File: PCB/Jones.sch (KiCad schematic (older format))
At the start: 246 parts, among them J1 USB_C_Receptacle_USB2.0, J2 Conn_01x03, J3 Conn_01x02, J5 Conn_02x03_Odd_Even, U1 ATmega32U4-AU, U2 24LC64, Y1 16MHz

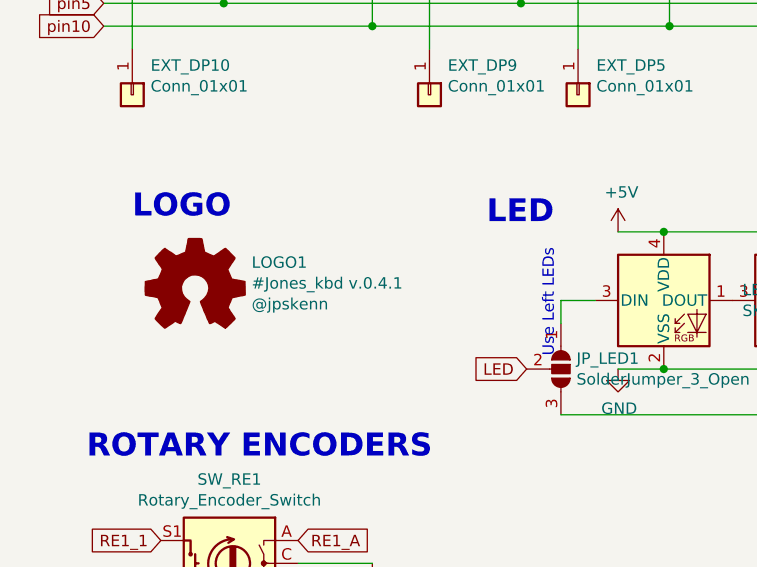
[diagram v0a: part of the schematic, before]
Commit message: 世界市民メッセージ追加。バージョン表記更新
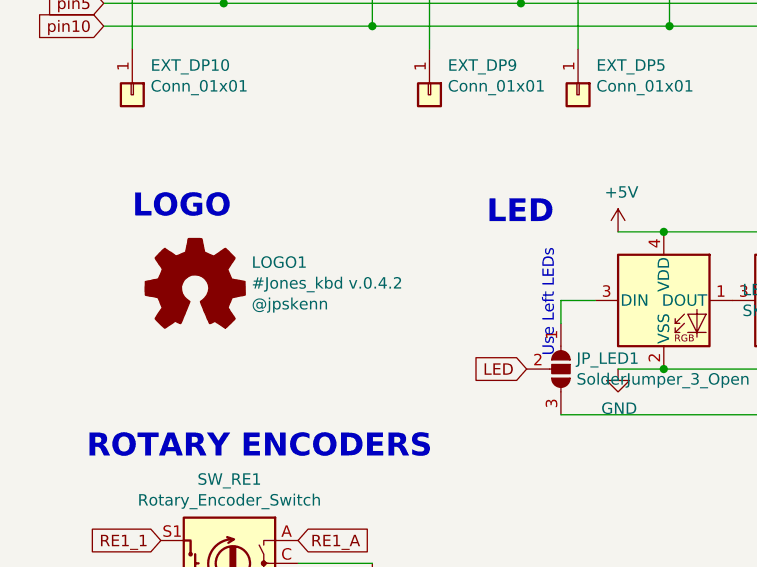
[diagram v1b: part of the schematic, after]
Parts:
- LOGO1: value #Jones_kbd v.0.4.1 -> #Jones_kbd v.0.4.2
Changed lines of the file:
@@
 Sheet 1 1
 Title "Jones"
-Date "2021-06-27"
-Rev "v.0.4.1"
+Date "2021-08-01"
+Rev "v.0.4.2"
 Comp "@jpskenn"
 Comment1 ""
@@
 P 1200 8675
 F 0 "LOGO1" H 1447 8791 50  0000 L CNN
-F 1 "#Jones_kbd v.0.4.1" H 1447 8700 50  0000 L CNN
+F 1 "#Jones_kbd v.0.4.2" H 1447 8700 50  0000 L CNN
 F 2 "locallib:Jones_logo_7.8x13.2" H 1200 8675 50  0001 C CNN
 F 3 "~" H 1200 8675 50  0001 C CNN

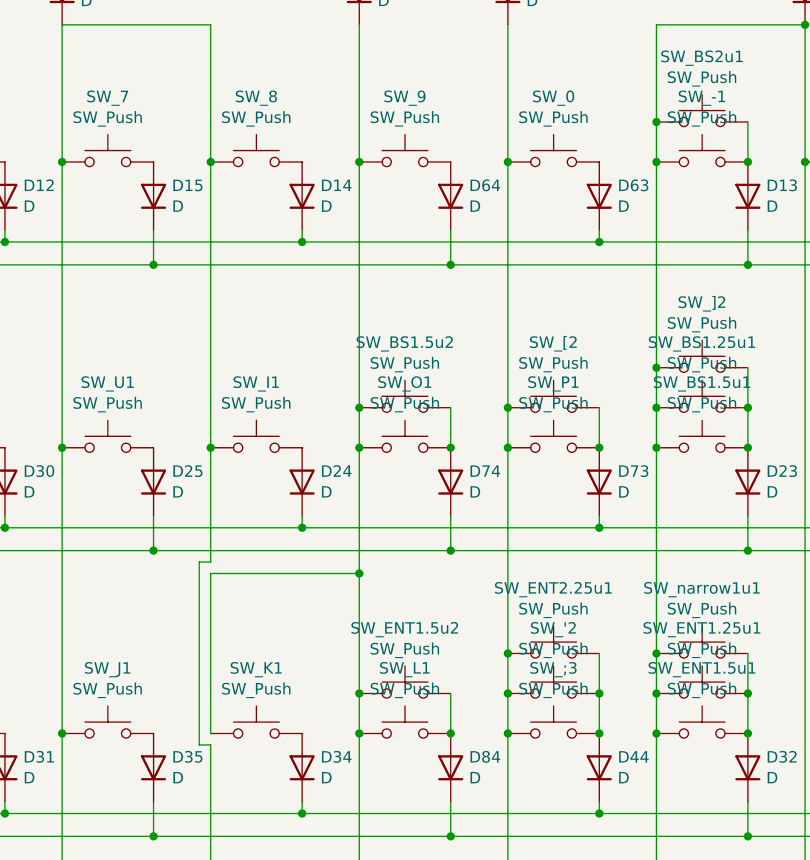
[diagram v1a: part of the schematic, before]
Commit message: Narrowレイアウトを、104USと108JPキーキャップに対応
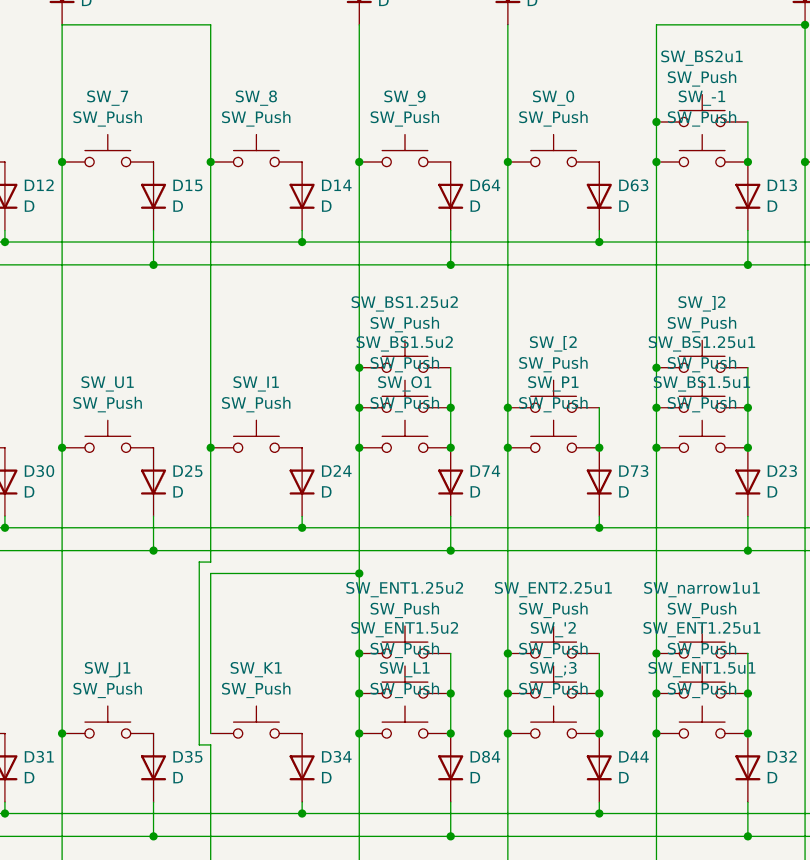
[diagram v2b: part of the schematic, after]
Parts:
- added SW_BS1.25u2, SW_ENT1.25u2: SW_Push, MX_Alps_Hybrid:MXOnly-1.25U-Hotswap-guide-Rotate, symbol Switch:SW_Push
- SW_BS1.5u2, SW_ENT1.5u2: footprint MX_Alps_Hybrid:MXOnly-1.5U-Hotswap-guide -> MX_Alps_Hybrid:MXOnly-1.5U-Hotswap-guide-Rotate
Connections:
- wire segments 427 -> 431
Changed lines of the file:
@@
 F 0 "SW_BS1.5u2" H 8275 3435 50  0000 C CNN
 F 1 "SW_Push" H 8275 3344 50  0000 C CNN
-F 2 "MX_Alps_Hybrid:MXOnly-1.5U-Hotswap-guide" H 8275 3350 50  0001 C CNN
+F 2 "MX_Alps_Hybrid:MXOnly-1.5U-Hotswap-guide-Rotate" H 8275 3350 50  0001 C CNN
 F 3 "~" H 8275 3350 50  0001 C CNN
 	1    8275 3150
@@
 	8075 3150 8075 3325
 Wire Wire Line
-	8075 2075 8075 3150
+	8075 2075 8075 2975
 $Comp
 L Switch:SW_Push SW_ENT1.5u2
@@
 F 0 "SW_ENT1.5u2" H 8275 4685 50  0000 C CNN
 F 1 "SW_Push" H 8275 4594 50  0000 C CNN
-F 2 "MX_Alps_Hybrid:MXOnly-1.5U-Hotswap-guide" H 8275 4600 50  0001 C CNN
+F 2 "MX_Alps_Hybrid:MXOnly-1.5U-Hotswap-guide-Rotate" H 8275 4600 50  0001 C CNN
 F 3 "~" H 8275 4600 50  0001 C CNN
 	1    8275 4400
@@
 	9125 4225 9125 4400
 Wire Wire Line
-	8075 3875 8075 4400
+	8075 3875 8075 4225
 Connection ~ 8725 4225
 Wire Wire Line
@@
 	1    0    0    -1
 $EndComp
+$Comp
+L Switch:SW_Push SW_BS1.25u2
+U 1 1 61379E30
+P 8275 2975
+F 0 "SW_BS1.25u2" H 8275 3260 50  0000 C CNN
+F 1 "SW_Push" H 8275 3169 50  0000 C CNN
+F 2 "MX_Alps_Hybrid:MXOnly-1.25U-Hotswap-guide-Rotate" H 8275 3175 50  0001 C CNN
+F 3 "~" H 8275 3175 50  0001 C CNN
+	1    8275 2975
+	1    0    0    -1
+$EndComp
+Connection ~ 8075 2975
+Wire Wire Line
+	8075 2975 8075 3150
+Wire Wire Line
+	8475 2975 8475 3150
+Connection ~ 8475 3150
+$Comp
+L Switch:SW_Push SW_ENT1.25u2
+U 1 1 613DB418
+P 8275 4225
+F 0 "SW_ENT1.25u2" H 8275 4510 50  0000 C CNN
+F 1 "SW_Push" H 8275 4419 50  0000 C CNN
+F 2 "MX_Alps_Hybrid:MXOnly-1.25U-Hotswap-guide-Rotate" H 8275 4425 50  0001 C CNN
+F 3 "~" H 8275 4425 50  0001 C CNN
+	1    8275 4225
+	1    0    0    -1
+$EndComp
+Connection ~ 8075 4225
+Wire Wire Line
+	8075 4225 8075 4400
+Wire Wire Line
+	8475 4225 8475 4400
+Connection ~ 8475 4400
 $EndSCHEMATC

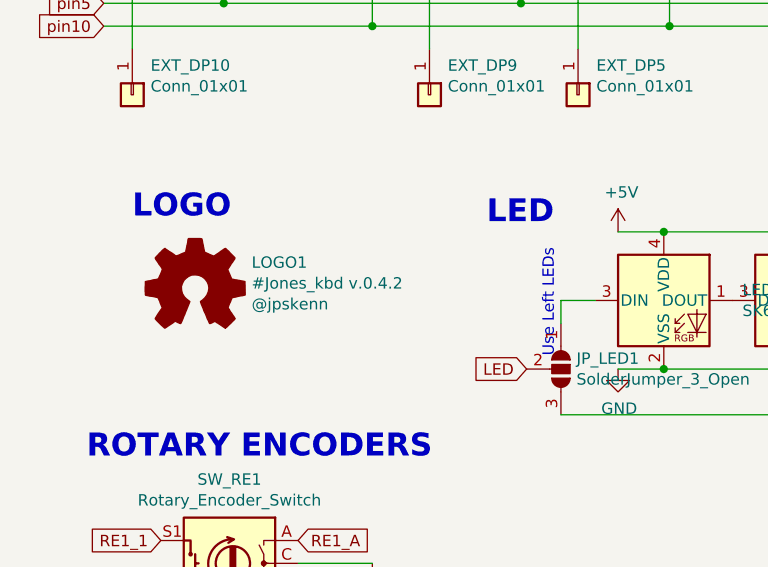
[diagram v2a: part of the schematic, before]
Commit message: バージョン表記変更
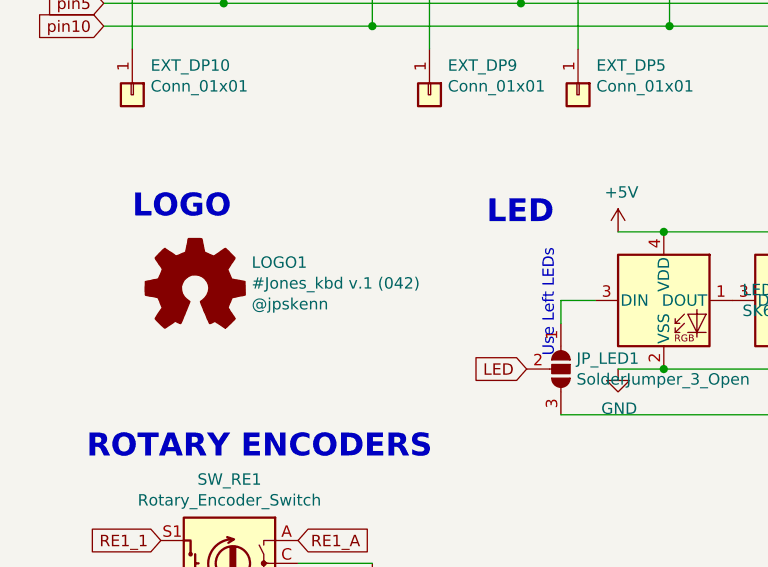
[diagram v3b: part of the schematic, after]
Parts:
- LOGO1: value #Jones_kbd v.0.4.2 -> #Jones_kbd v.1 (042)
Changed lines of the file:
@@
 Title "Jones"
 Date "2021-08-01"
-Rev "v.0.4.2"
+Rev "v.1 (042)"
 Comp "@jpskenn"
 Comment1 ""
@@
 P 1200 8675
 F 0 "LOGO1" H 1447 8791 50  0000 L CNN
-F 1 "#Jones_kbd v.0.4.2" H 1447 8700 50  0000 L CNN
+F 1 "#Jones_kbd v.1 (042)" H 1447 8700 50  0000 L CNN
 F 2 "locallib:Jones_logo_7.8x13.2" H 1200 8675 50  0001 C CNN
 F 3 "~" H 1200 8675 50  0001 C CNN

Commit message: 基板ロゴ更新
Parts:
- LOGO1: footprint locallib:Jones_logo_7.8x13.2 -> locallib:Jones_logo_B_R_60x98.2
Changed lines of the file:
@@
 F 0 "LOGO1" H 1447 8791 50  0000 L CNN
 F 1 "#Jones_kbd v.1 (042)" H 1447 8700 50  0000 L CNN
-F 2 "locallib:Jones_logo_7.8x13.2" H 1200 8675 50  0001 C CNN
+F 2 "locallib:Jones_logo_B_R_60x98.2" H 1200 8675 50  0001 C CNN
 F 3 "~" H 1200 8675 50  0001 C CNN
 F 4 "@jpskenn" H 1447 8609 50  0000 L CNN "Text"

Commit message: マトリクスのピン番号をQMKに合わせた
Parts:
- renumbered EXT_DP1 to EXT_DP0, EXT_DP2 to EXT_DP1, EXT_DP3 to EXT_DP2, EXT_DP4 to EXT_DP3, EXT_DP5 to EXT_DP4, EXT_DP6 to EXT_DP5, EXT_DP7 to EXT_DP6, EXT_DP8 to EXT_DP7, EXT_DP9 to EXT_DP8, EXT_DP10 to EXT_DP9, EXT_P1 to EXT_P0, EXT_P2 to EXT_P1, EXT_P3 to EXT_P2, EXT_P4 to EXT_P3, EXT_P5 to EXT_P4, EXT_P6 to EXT_P5, EXT_P7 to EXT_P6, EXT_P8 to EXT_P7, EXT_P9 to EXT_P8, EXT_P10 to EXT_P9
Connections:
- net labels added: pin0
- net labels removed: pin10
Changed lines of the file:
@@
 $EndComp
 Text GLabel 15275 2150 2    60   Input ~ 0
-pin6
-Text GLabel 15275 3750 2    60   Input ~ 0
 pin5
+Text GLabel 15275 3750 2    60   Input ~ 0
+pin4
 Text GLabel 15650 2450 2    50   Input ~ 0
-pin1
+pin0
 Wire Wire Line
 	13750 3450 14075 3450
@@
 $EndComp
 Text GLabel 800  2425 0    50   Input ~ 0
-pin1
+pin0
 Text GLabel 800  3675 0    50   Input ~ 0
-pin2
+pin1
 Text GLabel 800  4925 0    50   Input ~ 0
-pin3
+pin2
 Text GLabel 800  6175 0    50   Input ~ 0
-pin4
+pin3
 Text GLabel 800  7425 0    50   Input ~ 0
-pin5
+pin4
 Text GLabel 800  5025 0    50   Input ~ 0
-pin8
+pin7
 Text GLabel 800  6275 0    50   Input ~ 0
-pin9
+pin8
 Text GLabel 800  3775 0    50   Input ~ 0
-pin7
+pin6
 $Comp
 L Device:D D39
@@
 Connection ~ 9775 4575
 Text GLabel 4175 1175 1    50   Input ~ 0
-pin1
+pin0
 Text GLabel 10025 1175 1    50   Input ~ 0
-pin2
+pin1
 Text GLabel 6775 1175 1    50   Input ~ 0
-pin3
+pin2
 Text GLabel 8075 1175 1    50   Input ~ 0
-pin4
+pin3
 Text GLabel 2875 1175 1    50   Input ~ 0
-pin5
+pin4
 Text GLabel 6125 1175 1    50   Input ~ 0
-pin6
+pin5
 Text GLabel 8725 1175 1    50   Input ~ 0
-pin8
-Text GLabel 5475 1175 1    50   Input ~ 0
 pin7
-Text GLabel 800  2525 0    50   Input ~ 0
+Text GLabel 5475 1175 1    50   Input ~ 0
 pin6
+Text GLabel 800  2525 0    50   Input ~ 0
+pin5
 $Comp
 L Switch:SW_Push SW_RIGHT1
@@
 RE2_B
 Text GLabel 15275 2550 2    60   Input ~ 0
-pin9
-Text GLabel 15275 2850 2    60   Input ~ 0
 pin8
+Text GLabel 15275 2850 2    60   Input ~ 0
+pin7
 Connection ~ 3250 8425
 Wire Wire Line
@@
 AUDIO2
 Text GLabel 15275 4350 2    60   Input ~ 0
-pin3
+pin2
 Text GLabel 15275 4850 2    50   Input ~ 0
 RE2_A
@@
 LED
 Text GLabel 15275 3950 2    60   Input ~ 0
-pin4
+pin3
 Wire Wire Line
 	1325 2375 1325 2425
@@
 $EndComp
 Text GLabel 15275 4050 2    50   Input ~ 0
-pin10
+pin9
 Text GLabel 800  7525 0    50   Input ~ 0
-pin10
+pin9
 Wire Wire Line
 	800  2525 1975 2525
@@
 	800  7525 1975 7525
 Text GLabel 2225 1175 1    50   Input ~ 0
-pin9
+pin8
 $Comp
 L Device:D D9
@@
 $EndComp
 Text GLabel 925  1175 1    50   Input ~ 0
-pin10
+pin9
 $Comp
 L Device:D D42
@@
 SDA
 $Comp
-L Connector_Generic:Conn_01x01 EXT_P1
+L Connector_Generic:Conn_01x01 EXT_P0
 U 1 1 60A4B967
 P 10625 2425
-F 0 "EXT_P1" H 10705 2467 50  0000 L CNN
+F 0 "EXT_P0" H 10705 2467 50  0000 L CNN
 F 1 "Conn_01x01" H 10705 2376 50  0000 L CNN
 F 2 "TestPoint:TestPoint_THTPad_D1.5mm_Drill0.7mm" H 10625 2425 50  0001 C CNN
@@
 Connection ~ 10425 2425
 $Comp
-L Connector_Generic:Conn_01x01 EXT_P6
+L Connector_Generic:Conn_01x01 EXT_P5
 U 1 1 60A4CD39
 P 10625 2525
-F 0 "EXT_P6" H 10705 2567 50  0000 L CNN
+F 0 "EXT_P5" H 10705 2567 50  0000 L CNN
 F 1 "Conn_01x01" H 10705 2476 50  0000 L CNN
 F 2 "TestPoint:TestPoint_THTPad_D1.5mm_Drill0.7mm" H 10625 2525 50  0001 C CNN
@@
 Connection ~ 9775 2525
 $Comp
-L Connector_Generic:Conn_01x01 EXT_P2
+L Connector_Generic:Conn_01x01 EXT_P1
 U 1 1 60AB0114
 P 10625 3675
-F 0 "EXT_P2" H 10705 3717 50  0000 L CNN
+F 0 "EXT_P1" H 10705 3717 50  0000 L CNN
 F 1 "Conn_01x01" H 10705 3626 50  0000 L CNN
 F 2 "TestPoint:TestPoint_THTPad_D1.5mm_Drill0.7mm" H 10625 3675 50  0001 C CNN
@@
 $EndComp
 $Comp
-L Connector_Generic:Conn_01x01 EXT_P7
+L Connector_Generic:Conn_01x01 EXT_P6
 U 1 1 60AB011A
 P 10625 3775
-F 0 "EXT_P7" H 10705 3817 50  0000 L CNN
+F 0 "EXT_P6" H 10705 3817 50  0000 L CNN
 F 1 "Conn_01x01" H 10705 3726 50  0000 L CNN
 F 2 "TestPoint:TestPoint_THTPad_D1.5mm_Drill0.7mm" H 10625 3775 50  0001 C CNN
@@
 Connection ~ 9125 3675
 $Comp
-L Connector_Generic:Conn_01x01 EXT_P3
+L Connector_Generic:Conn_01x01 EXT_P2
 U 1 1 60B78AB4
 P 10625 4925
-F 0 "EXT_P3" H 10705 4967 50  0000 L CNN
+F 0 "EXT_P2" H 10705 4967 50  0000 L CNN
 F 1 "Conn_01x01" H 10705 4876 50  0000 L CNN
 F 2 "TestPoint:TestPoint_THTPad_D1.5mm_Drill0.7mm" H 10625 4925 50  0001 C CNN
@@
 $EndComp
 $Comp
-L Connector_Generic:Conn_01x01 EXT_P8
+L Connector_Generic:Conn_01x01 EXT_P7
 U 1 1 60B78ABA
 P 10625 5025
-F 0 "EXT_P8" H 10705 5067 50  0000 L CNN
+F 0 "EXT_P7" H 10705 5067 50  0000 L CNN
 F 1 "Conn_01x01" H 10705 4976 50  0000 L CNN
 F 2 "TestPoint:TestPoint_THTPad_D1.5mm_Drill0.7mm" H 10625 5025 50  0001 C CNN
@@
 Connection ~ 9775 5025
 $Comp
-L Connector_Generic:Conn_01x01 EXT_P4
+L Connector_Generic:Conn_01x01 EXT_P3
 U 1 1 60C0E797
 P 10625 6175
-F 0 "EXT_P4" H 10705 6217 50  0000 L CNN
+F 0 "EXT_P3" H 10705 6217 50  0000 L CNN
 F 1 "Conn_01x01" H 10705 6126 50  0000 L CNN
 F 2 "TestPoint:TestPoint_THTPad_D1.5mm_Drill0.7mm" H 10625 6175 50  0001 C CNN
@@
 $EndComp
 $Comp
-L Connector_Generic:Conn_01x01 EXT_P9
+L Connector_Generic:Conn_01x01 EXT_P8
 U 1 1 60C0E79D
 P 10625 6275
-F 0 "EXT_P9" H 10705 6317 50  0000 L CNN
+F 0 "EXT_P8" H 10705 6317 50  0000 L CNN
 F 1 "Conn_01x01" H 10705 6226 50  0000 L CNN
 F 2 "TestPoint:TestPoint_THTPad_D1.5mm_Drill0.7mm" H 10625 6275 50  0001 C CNN
@@
 Connection ~ 9775 6275
 $Comp
-L Connector_Generic:Conn_01x01 EXT_P5
+L Connector_Generic:Conn_01x01 EXT_P4
 U 1 1 60C7253E
 P 10625 7425
-F 0 "EXT_P5" H 10705 7467 50  0000 L CNN
+F 0 "EXT_P4" H 10705 7467 50  0000 L CNN
 F 1 "Conn_01x01" H 10705 7376 50  0000 L CNN
 F 2 "TestPoint:TestPoint_THTPad_D1.5mm_Drill0.7mm" H 10625 7425 50  0001 C CNN
@@
 $EndComp
 $Comp
-L Connector_Generic:Conn_01x01 EXT_P10
+L Connector_Generic:Conn_01x01 EXT_P9
 U 1 1 60C72544
 P 10625 7525
-F 0 "EXT_P10" H 10705 7567 50  0000 L CNN
+F 0 "EXT_P9" H 10705 7567 50  0000 L CNN
 F 1 "Conn_01x01" H 10705 7476 50  0000 L CNN
 F 2 "TestPoint:TestPoint_THTPad_D1.5mm_Drill0.7mm" H 10625 7525 50  0001 C CNN
@@
 	10425 7525 9775 7525
 Connection ~ 9775 7525
-$Comp
-L Connector_Generic:Conn_01x01 EXT_DP10
-U 1 1 60CD6E89
-P 925 7825
-F 0 "EXT_DP10" V 797 7905 50  0000 L CNN
-F 1 "Conn_01x01" V 888 7905 50  0000 L CNN
-F 2 "TestPoint:TestPoint_THTPad_D1.5mm_Drill0.7mm" H 925 7825 50  0001 C CNN
-F 3 "~" H 925 7825 50  0001 C CNN
-	1    925  7825
-	0    1    1    0
-$EndComp
 Wire Wire Line
 	925  7075 925  7625
 Connection ~ 925  7075
 $Comp
-L Connector_Generic:Conn_01x01 EXT_DP9
+L Connector_Generic:Conn_01x01 EXT_DP8
 U 1 1 60DD63ED
 P 2225 7825
-F 0 "EXT_DP9" V 2097 7905 50  0000 L CNN
+F 0 "EXT_DP8" V 2097 7905 50  0000 L CNN
 F 1 "Conn_01x01" V 2188 7905 50  0000 L CNN
 F 2 "TestPoint:TestPoint_THTPad_D1.5mm_Drill0.7mm" H 2225 7825 50  0001 C CNN
@@
 $EndComp
 $Comp
-L Connector_Generic:Conn_01x01 EXT_DP5
+L Connector_Generic:Conn_01x01 EXT_DP4
 U 1 1 60E07EE7
 P 2875 7825
-F 0 "EXT_DP5" V 2747 7905 50  0000 L CNN
+F 0 "EXT_DP4" V 2747 7905 50  0000 L CNN
 F 1 "Conn_01x01" V 2838 7905 50  0000 L CNN
 F 2 "TestPoint:TestPoint_THTPad_D1.5mm_Drill0.7mm" H 2875 7825 50  0001 C CNN
@@
 $EndComp
 $Comp
-L Connector_Generic:Conn_01x01 EXT_DP1
+L Connector_Generic:Conn_01x01 EXT_DP0
 U 1 1 60E7FA4E
 P 4175 7825
-F 0 "EXT_DP1" V 4047 7905 50  0000 L CNN
+F 0 "EXT_DP0" V 4047 7905 50  0000 L CNN
 F 1 "Conn_01x01" V 4138 7905 50  0000 L CNN
 F 2 "TestPoint:TestPoint_THTPad_D1.5mm_Drill0.7mm" H 4175 7825 50  0001 C CNN
@@
 $EndComp
 $Comp
-L Connector_Generic:Conn_01x01 EXT_DP7
+L Connector_Generic:Conn_01x01 EXT_DP6
 U 1 1 60EB18EB
 P 5475 7825
-F 0 "EXT_DP7" V 5347 7905 50  0000 L CNN
+F 0 "EXT_DP6" V 5347 7905 50  0000 L CNN
 F 1 "Conn_01x01" V 5438 7905 50  0000 L CNN
 F 2 "TestPoint:TestPoint_THTPad_D1.5mm_Drill0.7mm" H 5475 7825 50  0001 C CNN
@@
 $EndComp
 $Comp
-L Connector_Generic:Conn_01x01 EXT_DP6
+L Connector_Generic:Conn_01x01 EXT_DP5
 U 1 1 60EE36D9
 P 6125 7825
-F 0 "EXT_DP6" V 5997 7905 50  0000 L CNN
+F 0 "EXT_DP5" V 5997 7905 50  0000 L CNN
 F 1 "Conn_01x01" V 6088 7905 50  0000 L CNN
 F 2 "TestPoint:TestPoint_THTPad_D1.5mm_Drill0.7mm" H 6125 7825 50  0001 C CNN
@@
 $EndComp
 $Comp
-L Connector_Generic:Conn_01x01 EXT_DP3
+L Connector_Generic:Conn_01x01 EXT_DP2
 U 1 1 60F1572E
 P 6775 7825
-F 0 "EXT_DP3" V 6647 7905 50  0000 L CNN
+F 0 "EXT_DP2" V 6647 7905 50  0000 L CNN
 F 1 "Conn_01x01" V 6738 7905 50  0000 L CNN
 F 2 "TestPoint:TestPoint_THTPad_D1.5mm_Drill0.7mm" H 6775 7825 50  0001 C CNN
@@
 $EndComp
 $Comp
-L Connector_Generic:Conn_01x01 EXT_DP4
+L Connector_Generic:Conn_01x01 EXT_DP3
 U 1 1 60F4752D
 P 8075 7825
-F 0 "EXT_DP4" V 7947 7905 50  0000 L CNN
+F 0 "EXT_DP3" V 7947 7905 50  0000 L CNN
 F 1 "Conn_01x01" V 8038 7905 50  0000 L CNN
 F 2 "TestPoint:TestPoint_THTPad_D1.5mm_Drill0.7mm" H 8075 7825 50  0001 C CNN
@@
 $EndComp
 $Comp
-L Connector_Generic:Conn_01x01 EXT_DP8
+L Connector_Generic:Conn_01x01 EXT_DP7
 U 1 1 60F795D2
 P 8725 7825
-F 0 "EXT_DP8" V 8597 7905 50  0000 L CNN
+F 0 "EXT_DP7" V 8597 7905 50  0000 L CNN
 F 1 "Conn_01x01" V 8688 7905 50  0000 L CNN
 F 2 "TestPoint:TestPoint_THTPad_D1.5mm_Drill0.7mm" H 8725 7825 50  0001 C CNN
@@
 $EndComp
 $Comp
-L Connector_Generic:Conn_01x01 EXT_DP2
+L Connector_Generic:Conn_01x01 EXT_DP1
 U 1 1 60FAB664
 P 10025 7825
-F 0 "EXT_DP2" V 9897 7905 50  0000 L CNN
+F 0 "EXT_DP1" V 9897 7905 50  0000 L CNN
 F 1 "Conn_01x01" V 9988 7905 50  0000 L CNN
 F 2 "TestPoint:TestPoint_THTPad_D1.5mm_Drill0.7mm" H 10025 7825 50  0001 C CNN
@@
 	9125 4925 10425 4925
 Text GLabel 15650 2150 2    50   Input ~ 0
-pin7
+pin6
 Text GLabel 15650 2350 2    50   Input ~ 0
-pin2
+pin1
 Text GLabel 15650 2250 2    50   Input ~ 0
 MOSI
@@
 	8475 4225 8475 4400
 Connection ~ 8475 4400
+$Comp
+L Connector_Generic:Conn_01x01 EXT_DP9
+U 1 1 60CD6E89
+P 925 7825
+F 0 "EXT_DP9" V 797 7905 50  0000 L CNN
+F 1 "Conn_01x01" V 888 7905 50  0000 L CNN
+F 2 "TestPoint:TestPoint_THTPad_D1.5mm_Drill0.7mm" H 925 7825 50  0001 C CNN
+F 3 "~" H 925 7825 50  0001 C CNN
+	1    925  7825
+	0    1    1    0
+$EndComp
 $EndSCHEMATC

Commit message: 配線調整
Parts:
- removed U1: ATmega32U4-AU, Package_QFP:TQFP-44_10x10mm_P0.8mm, symbol MCU_Microchip_ATmega:ATmega32U4-AU
- added U1: ATmega32U4-MU, Housings_DFN_QFN:QFN-44-1EP_7x7mm_Pitch0.5mm, symbol MCU_Microchip_ATmega:ATmega32U4-MU
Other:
- moved on the sheet: C2, C3, C6, R5, R6, ResetSW1, Y1

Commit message: ATmega32u4-MUのSMTA品番を記入
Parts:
- U1: LCSC (none) -> C45874
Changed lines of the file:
@@
 F 2 "Housings_DFN_QFN:QFN-44-1EP_7x7mm_Pitch0.5mm" H 14725 3375 50  0001 C CIN
 F 3 "http://ww1.microchip.com/downloads/en/DeviceDoc/Atmel-7766-8-bit-AVR-ATmega16U4-32U4_Datasheet.pdf" H 14725 3375 50  0001 C CNN
+F 4 "C45874" H 14725 3375 50  0001 C CNN "LCSC"
 	1    14725 3375
 	1    0    0    -1
